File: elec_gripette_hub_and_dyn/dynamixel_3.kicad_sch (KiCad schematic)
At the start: 25 parts, among them J4 Dynamixel-3, J5 Dynamixel-3, Q1 MMBT3906, U3 CH343P, U4 SN74LVC1G125DBV, U5 SN74LVC1G126DBVR

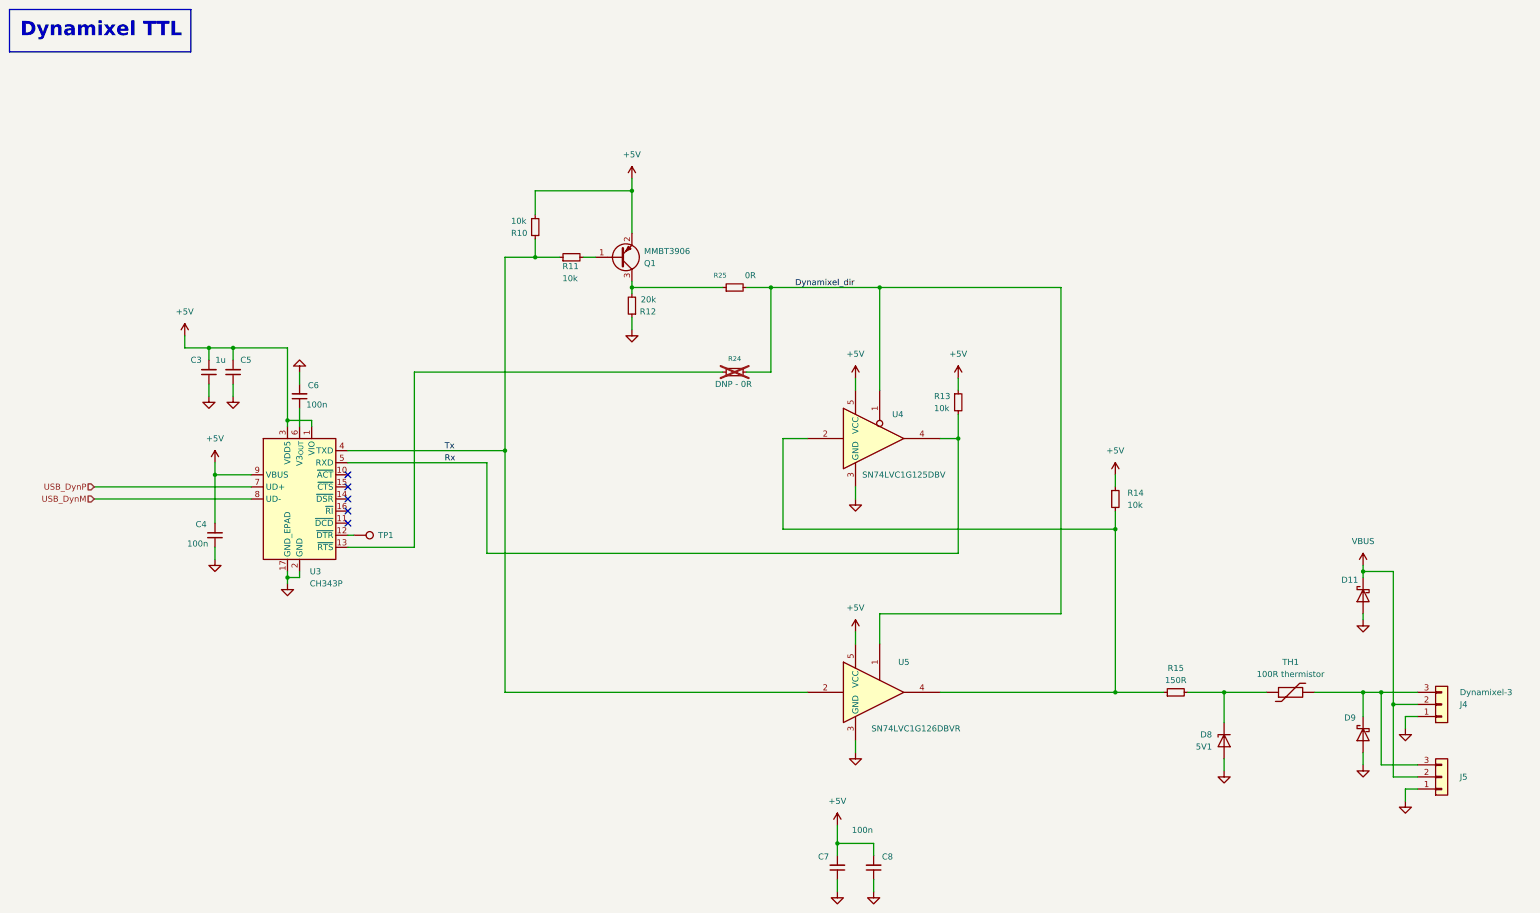
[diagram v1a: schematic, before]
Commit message: [update] Gripette hub routed
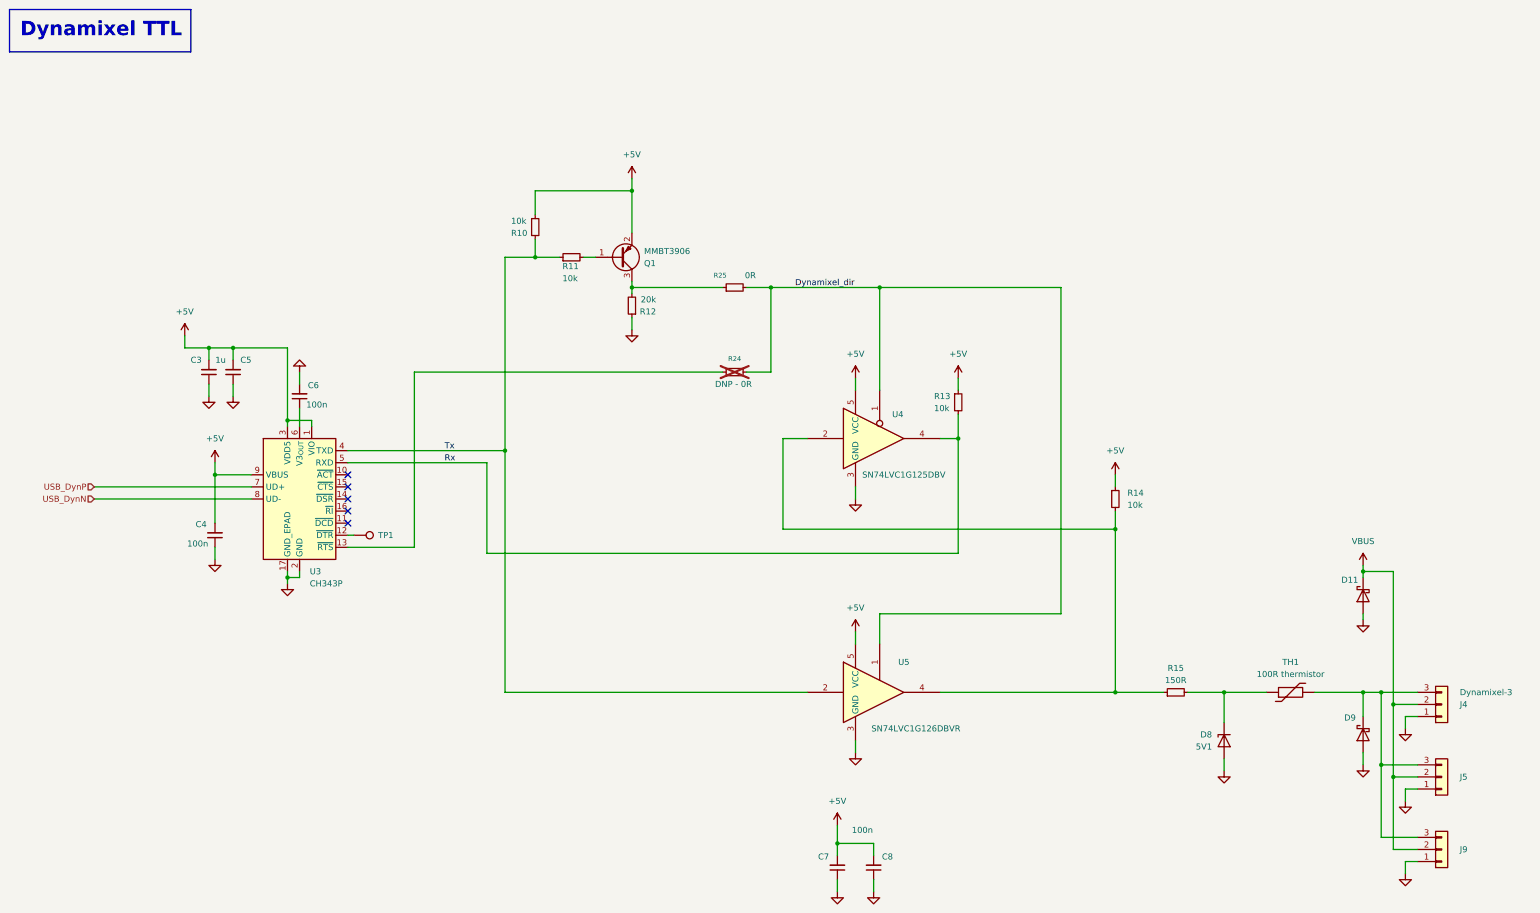
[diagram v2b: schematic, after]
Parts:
- added J9: Dynamixel-3, Connector_JST:JST_EH_B3B-EH-A_1x03_P2.50mm_Vertical, symbol Connector_Generic:Conn_01x03
- J4, J5: footprint Connector_JST:JST_EH_S3B-EH_1x03_P2.50mm_Horizontal -> Connector_JST:JST_EH_B3B-EH-A_1x03_P2.50mm_Vertical; LCSC Part C263754 -> (none)
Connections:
- net GND: now also J9.1 (Pin_1)
- net VBUS: now also J9.2 (Pin_2)
- net at D9.1 (K), J4.3 (Pin_3), J5.3 (Pin_3)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: now also J9.3 (Pin_3)
- net USB_DynM renamed USB_DynN

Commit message: [uptate] Gripette hub ok for JLC
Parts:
- D11, D9: FT Rotation Offset 180 -> (none); LCSC Part C78734 -> C64886
- J4, J5, J9: FT Rotation Offset 180 -> (none); LCSC Part (none) -> C160259
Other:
- company: Pollen Robotics / Hugging Face -> Pollen Robotics/HF
- title: elec_maroilles -> Grippette - USB hub and Dynamixel device
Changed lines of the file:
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@@
 	(paper "A3")
 	(title_block
-		(title "elec_maroilles")
-		(date "2026-02-02")
-		(rev "B1")
-		(company "Pollen Robotics / Hugging Face")
+		(title "Grippette - USB hub and Dynamixel device")
+		(date "2026-04-16")
+		(rev "A1")
+		(company "Pollen Robotics/HF")
 	)
 	(text_box "Dynamixel TTL"
@@
 			)
 		)
-		(property "FT Rotation Offset" "180"
+		(property "FT Rotation Offset" ""
 			(at 317.5 153.67 90)
 			(effects
@@
 			)
 		)
-		(property "LCSC Part" "C78734"
+		(property "LCSC Part" "C64886"
 			(at 317.5 153.67 90)
 			(effects
@@
 			)
 		)
-		(property "LCSC Part" ""
+		(property "LCSC Part" "C160259"
 			(at 334.01 176.53 0)
 			(effects
@@
 			)
 		)
-		(property "FT Rotation Offset" "180"
+		(property "FT Rotation Offset" ""
 			(at 334.01 176.53 0)
 			(effects
@@
 			)
 		)
-		(property "LCSC Part" ""
+		(property "LCSC Part" "C160259"
 			(at 334.01 207.01 0)
 			(effects
@@
 			)
 		)
-		(property "FT Rotation Offset" "180"
+		(property "FT Rotation Offset" ""
 			(at 334.01 207.01 0)
 			(effects
@@
 			)
 		)
-		(property "LCSC Part" ""
+		(property "LCSC Part" "C160259"
 			(at 334.01 191.77 0)
 			(effects
@@
 			)
 		)
-		(property "FT Rotation Offset" "180"
+		(property "FT Rotation Offset" ""
 			(at 334.01 191.77 0)
 			(effects
@@
 			)
 		)
-		(property "FT Rotation Offset" "180"
+		(property "FT Rotation Offset" ""
 			(at 317.5 182.88 90)
 			(effects
@@
 			)
 		)
-		(property "LCSC Part" "C78734"
+		(property "LCSC Part" "C64886"
 			(at 317.5 182.88 90)
 			(effects

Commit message: [update] SCH B1-RC1
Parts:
- added R17, R29: 0R, Resistor_SMD:R_0402_1005Metric, symbol Device:R_Small
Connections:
- net Rx: now also R29.2; no longer U3.5 (RXD)
- net Tx: now also R17.2; no longer U3.4 (TXD)
- net Dyn_data: now reaches D9.1 (K), J4.3 (Pin_3), J5.3 (Pin_3), J9.3 (Pin_3), TH1.2
- new net: R29.1, U3.5 (RXD)
- new net: R17.1, U3.4 (TXD)
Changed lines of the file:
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@@
 	(title_block
 		(title "Grippette - USB hub and Dynamixel device")
-		(date "2026-04-16")
-		(rev "A1")
+		(date "2026-05-27")
+		(rev "B1")
 		(company "Pollen Robotics/HF")
 	)
@@
 	)
 	(junction
+		(at 311.15 173.99)
+		(diameter 0)
+		(color 0 0 0 0)
+	)
+	(junction
 		(at 215.9 88.9)
 		(diameter 0)
@@
 	(wire
 		(pts
+			(xy 114.3 123.19) (xy 137.16 123.19)
+		)
+		(stroke
+			(width 0)
+			(type default)
+		)
+	)
+	(wire
+		(pts
 			(xy 328.93 189.23) (xy 321.31 189.23)
 		)
@@
 	(wire
 		(pts
+			(xy 114.3 125.73) (xy 133.35 125.73)
+		)
+		(stroke
+			(width 0)
+			(type default)
+		)
+	)
+	(wire
+		(pts
 			(xy 207.01 205.74) (xy 207.01 208.28)
 		)
@@
 	(wire
 		(pts
-			(xy 104.14 125.73) (xy 133.35 125.73)
+			(xy 104.14 125.73) (xy 109.22 125.73)
 		)
 		(stroke
@@
 	(wire
 		(pts
-			(xy 307.34 173.99) (xy 317.5 173.99)
+			(xy 307.34 173.99) (xy 311.15 173.99)
 		)
 		(stroke
@@
 	(wire
 		(pts
+			(xy 312.42 171.45) (xy 311.15 171.45)
+		)
+		(stroke
+			(width 0)
+			(type default)
+		)
+	)
+	(wire
+		(pts
 			(xy 228.6 120.65) (xy 232.41 120.65)
 		)
@@
 	(wire
 		(pts
-			(xy 104.14 123.19) (xy 137.16 123.19)
+			(xy 104.14 123.19) (xy 109.22 123.19)
 		)
 		(stroke
@@
 	(wire
 		(pts
+			(xy 311.15 171.45) (xy 311.15 173.99)
+		)
+		(stroke
+			(width 0)
+			(type default)
+		)
+	)
+	(wire
+		(pts
 			(xy 91.44 101.6) (xy 91.44 116.84)
 		)
@@
 	(wire
 		(pts
+			(xy 311.15 173.99) (xy 317.5 173.99)
+		)
+		(stroke
+			(width 0)
+			(type default)
+		)
+	)
+	(wire
+		(pts
 			(xy 215.9 88.9) (xy 215.9 110.49)
 		)
@@
 	)
 	(label "Rx"
-		(at 124.46 125.73 0)
+		(at 127 125.73 0)
 		(effects
 			(font
@@
 	)
 	(label "Tx"
-		(at 124.46 123.19 0)
+		(at 127 123.19 0)
 		(effects
 			(font
@@
 		)
 	)
+	(hierarchical_label "Dyn_data"
+		(shape input)
+		(at 312.42 171.45 0)
+		(effects
+			(font
+				(size 1.27 1.27)
+			)
+			(justify left)
+		)
+	)
 	(symbol
 		(lib_id "Device:R_Small")
@@
 	)
 	(symbol
+		(lib_id "Device:R_Small")
+		(at 111.76 125.73 90)
+		(unit 1)
+		(exclude_from_sim no)
+		(in_bom yes)
+		(on_board yes)
+		(dnp no)
+		(property "Reference" "R29"
+			(at 107.95 124.714 90)
+			(effects
+				(font
+					(size 1.016 1.016)
+				)
+			)
+		)
+		(property "Value" "0R"
+			(at 115.316 124.714 90)
+			(effects
+				(font
+					(size 1.27 1.27)
+				)
+			)
+		)
+		(property "Footprint" "Resistor_SMD:R_0402_1005Metric"
+			(at 111.76 125.73 0)
+			(effects
+				(font
+					(size 1.27 1.27)
+				)
+				(hide yes)
+			)
+		)
+		(property "Datasheet" "~"
+			(at 111.76 125.73 0)
+			(effects
+				(font
+					(size 1.27 1.27)
+				)
+				(hide yes)
+			)
+		)
+		(property "Description" "Resistor, small symbol"
+			(at 111.76 125.73 0)
+			(effects
+				(font
+					(size 1.27 1.27)
+				)
+				(hide yes)
+			)
+		)
+		(property "LCSC Part" "C17168"
+			(at 111.76 125.73 90)
+			(effects
+				(font
+					(size 1.27 1.27)
+				)
+				(hide yes)
+			)
+		)
+		(pin "2"
+		)
+		(pin "1"
+		)
+		(instances
+			(project "elec_gripette_hub_and_dyn"
+				(path "/bc05f5da-608c-4912-90e4-36b13d989976/edad0453-e3dd-48f4-9e65-34ff832c5255"
+					(reference "R29")
+					(unit 1)
+				)
+			)
+		)
+	)
+	(symbol
 		(lib_id "power:GND")
 		(at 80.01 111.76 0)
@@
 					(unit 1)
 				)
+			)
+		)
+	)
+	(symbol
+		(lib_id "Device:R_Small")
+		(at 111.76 123.19 90)
+		(unit 1)
+		(exclude_from_sim no)
+		(in_bom yes)
+		(on_board yes)
+		(dnp no)
+		(property "Reference" "R17"
+			(at 107.95 122.174 90)
+			(effects
+				(font
+					(size 1.016 1.016)
+				)
+			)
+		)
+		(property "Value" "0R"
+			(at 115.316 122.174 90)
+			(effects
+				(font
+					(size 1.27 1.27)
+				)
+			)
+		)
+		(property "Footprint" "Resistor_SMD:R_0402_1005Metric"
+			(at 111.76 123.19 0)
+			(effects
+				(font
+					(size 1.27 1.27)
+				)
+				(hide yes)
+			)
+		)
+		(property "Datasheet" "~"
+			(at 111.76 123.19 0)
+			(effects
+				(font
+					(size 1.27 1.27)
+				)
+				(hide yes)
+			)
+		)
+		(property "Description" "Resistor, small symbol"
+			(at 111.76 123.19 0)
+			(effects
+				(font
+					(size 1.27 1.27)
+				)
+				(hide yes)
+			)
+		)
+		(property "LCSC Part" "C17168"
+			(at 111.76 123.19 90)
+			(effects
+				(font
+					(size 1.27 1.27)
+				)
+				(hide yes)
+			)
+		)
+		(pin "2"
+		)
+		(pin "1"
+		)
+		(instances
+			(project "elec_gripette_hub_and_dyn"
+				(path "/bc05f5da-608c-4912-90e4-36b13d989976/edad0453-e3dd-48f4-9e65-34ff832c5255"
+					(reference "R17")
+					(unit 1)
+				)

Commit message: [update] SCH + PCB B1-RC1
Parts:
- removed TP1: TestPoint, TestPoint:TestPoint_Pad_D1.0mm, symbol Connector:TestPoint
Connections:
- net USB_DynN renamed hub_DP2-
- net USB_DynP renamed hub_DP2+
- no-connect marks 5 -> 6
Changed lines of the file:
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@@
 	)
 	(no_connect
+		(at 104.14 140.97)
+	)
+	(no_connect
 		(at 104.14 138.43)
 	)
@@
 	(wire
 		(pts
-			(xy 105.41 140.97) (xy 104.14 140.97)
-		)
-		(stroke
-			(width 0)
-			(type default)
-		)
-	)
-	(wire
-		(pts
 			(xy 214.63 205.74) (xy 207.01 205.74)
 		)
@@
 		)
 	)
-	(hierarchical_label "USB_DynN"
+	(hierarchical_label "hub_DP2-"
 		(shape input)
 		(at 50.8 133.35 180)
@@
 		)
 	)
-	(hierarchical_label "USB_DynP"
+	(hierarchical_label "hub_DP2+"
 		(shape input)
 		(at 50.8 130.81 180)
@@
 					(unit 1)
 				)
-			)
-		)
-	)
-	(symbol
-		(lib_id "Connector:TestPoint")
-		(at 105.41 140.97 270)
-		(unit 1)
-		(exclude_from_sim no)
-		(in_bom yes)
-		(on_board yes)
-		(dnp no)
-		(fields_autoplaced yes)
-		(property "Reference" "TP1"
-			(at 110.49 140.9699 90)
-			(effects
-				(font
-					(size 1.27 1.27)
-				)
-				(justify left)
-			)
-		)
-		(property "Value" "TestPoint"
-			(at 110.49 142.2399 90)
-			(effects
-				(font
-					(size 1.27 1.27)
-				)
-				(justify left)
-				(hide yes)
-			)
-		)
-		(property "Footprint" "TestPoint:TestPoint_Pad_D1.0mm"
-			(at 105.41 146.05 0)
-			(effects
-				(font
-					(size 1.27 1.27)
-				)
-				(hide yes)
-			)
-		)
-		(property "Datasheet" "~"
-			(at 105.41 146.05 0)
-			(effects
-				(font
-					(size 1.27 1.27)
-				)
-				(hide yes)
-			)
-		)
-		(property "Description" "test point"
-			(at 105.41 140.97 0)
-			(effects
-				(font
-					(size 1.27 1.27)
-				)
-				(hide yes)
-			)
-		)
-		(property "Field7" ""
-			(at 105.41 140.97 90)
-			(effects
-				(font
-					(size 1.27 1.27)
-				)
-				(hide yes)
-			)
-		)
-		(pin "1"
-		)
-		(instances
-			(project "elec_gripette_hub_and_dyn"
-				(path "/bc05f5da-608c-4912-90e4-36b13d989976/edad0453-e3dd-48f4-9e65-34ff832c5255"
-					(reference "TP1")
-					(unit 1)
-				)

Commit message: [update] Before review
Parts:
- R24: value DNP - 0R -> DNP-0R; footprint Resistor_SMD:R_0402_1005Metric -> Resistor_SMD:R_0603_1608Metric; LCSC Part C17168 -> (none)
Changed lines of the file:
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@@
 			)
 		)
-		(property "Value" "DNP - 0R"
+		(property "Value" "DNP-0R"
 			(at 185.166 109.22 90)
 			(effects
@@
 			)
 		)
-		(property "Footprint" "Resistor_SMD:R_0402_1005Metric"
+		(property "Footprint" "Resistor_SMD:R_0603_1608Metric"
 			(at 185.42 106.68 0)
 			(effects
@@
 			)
 		)
-		(property "LCSC Part" "C17168"
+		(property "LCSC Part" ""
 			(at 185.42 106.68 90)
 			(effects

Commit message: [update] gripette + bulkhead -B1 in production @JLCPCB
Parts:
- removed J4: Dynamixel-3, Connector_JST:JST_EH_B3B-EH-A_1x03_P2.50mm_Vertical, symbol Connector_Generic:Conn_01x03
- J5: value Dynamixel-3 -> Feetech; footprint Connector_JST:JST_EH_B3B-EH-A_1x03_P2.50mm_Vertical -> Connector_Molex:Molex_SPOX_5267-03A_1x03_P2.50mm_Vertical; FT Rotation Offset (none) -> 180; LCSC Part C160259 -> C293315; Man. JST -> (none); Man. Ref. B3B-EH-A(LF)(SN) -> (none)
- J9: value Dynamixel-3 -> Feetech; footprint Connector_JST:JST_EH_B3B-EH-A_1x03_P2.50mm_Vertical -> Connector_Molex:Molex_SPOX_5267-03A_1x03_P2.50mm_Vertical; FT Rotation Offset (none) -> 180; LCSC Part C160259 -> (none); Man. JST -> (none); Man. Ref. B3B-EH-A(LF)(SN) -> (none); now not fitted
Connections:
- net Dyn_data: now also J5.1 (Pin_1), J9.1 (Pin_1); no longer J5.3 (Pin_3), J9.3 (Pin_3)
- net GND: now also J5.3 (Pin_3), J9.3 (Pin_3); no longer J5.1 (Pin_1), J9.1 (Pin_1)
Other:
- moved on the sheet: J5
